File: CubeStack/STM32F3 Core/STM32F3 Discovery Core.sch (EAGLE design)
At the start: 46 parts, among them IC1 FT230XQ, Q1 FC-12M, Q2 MBT3904DW2T1, Q3 MBT3904DW2T1

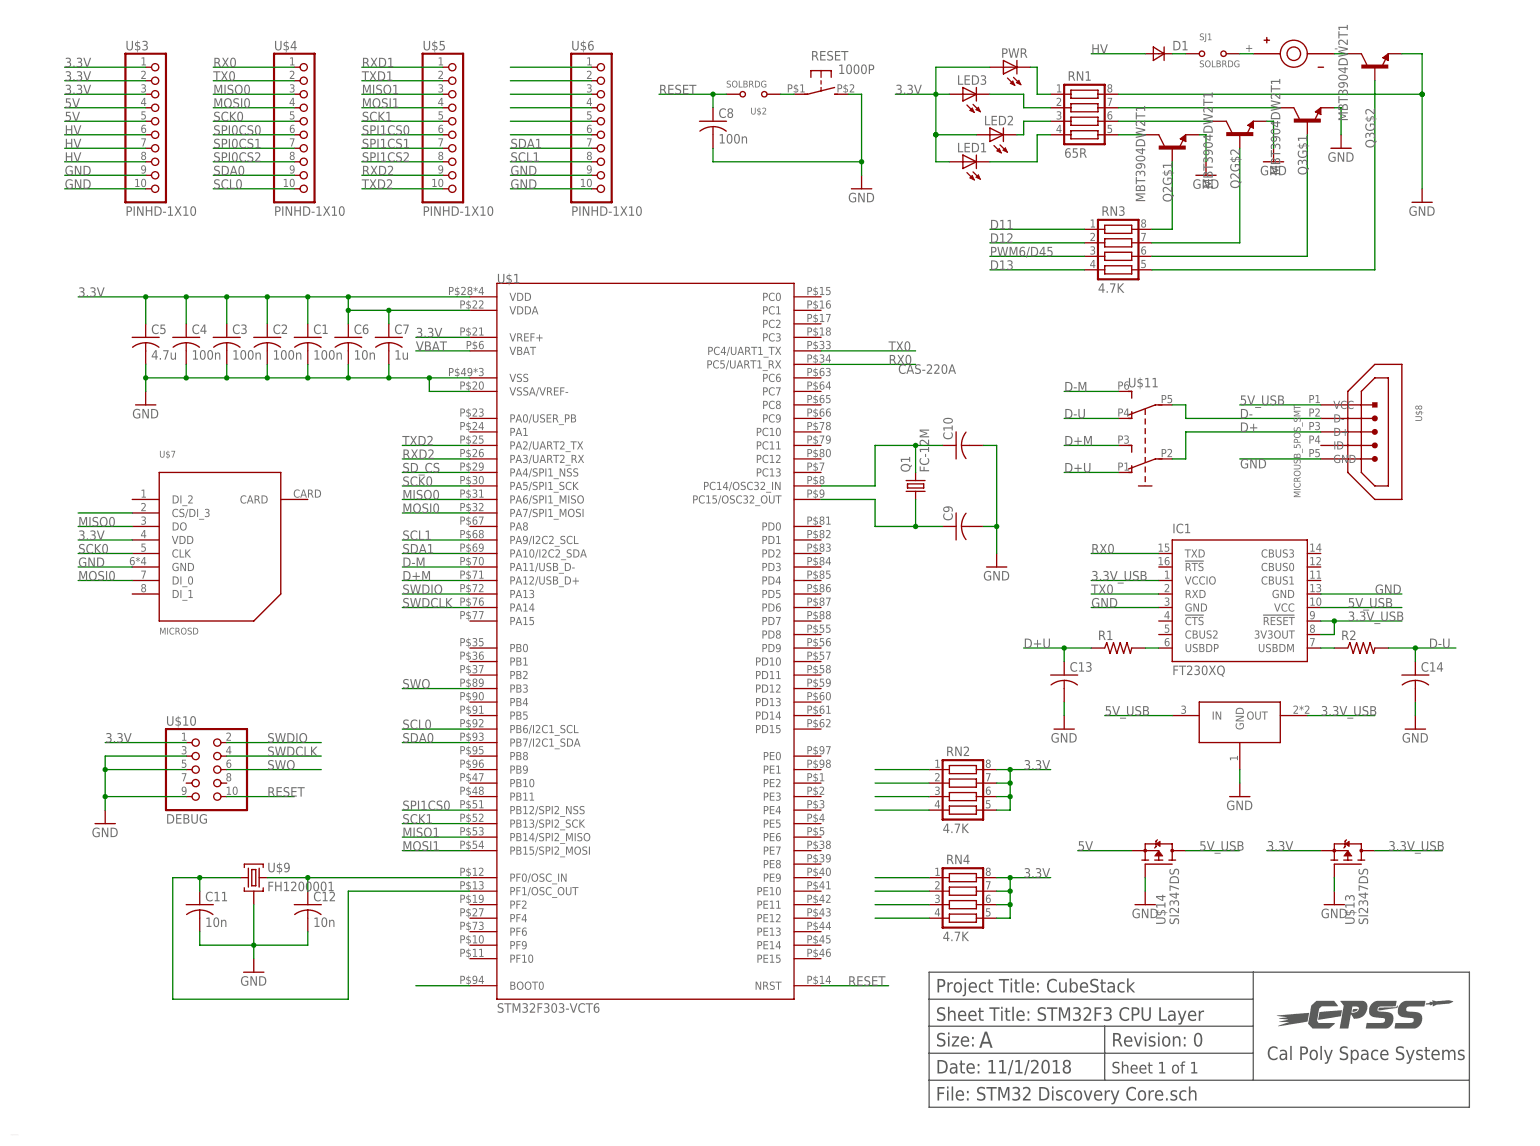
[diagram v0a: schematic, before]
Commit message: Routed PWM, GPIO lines
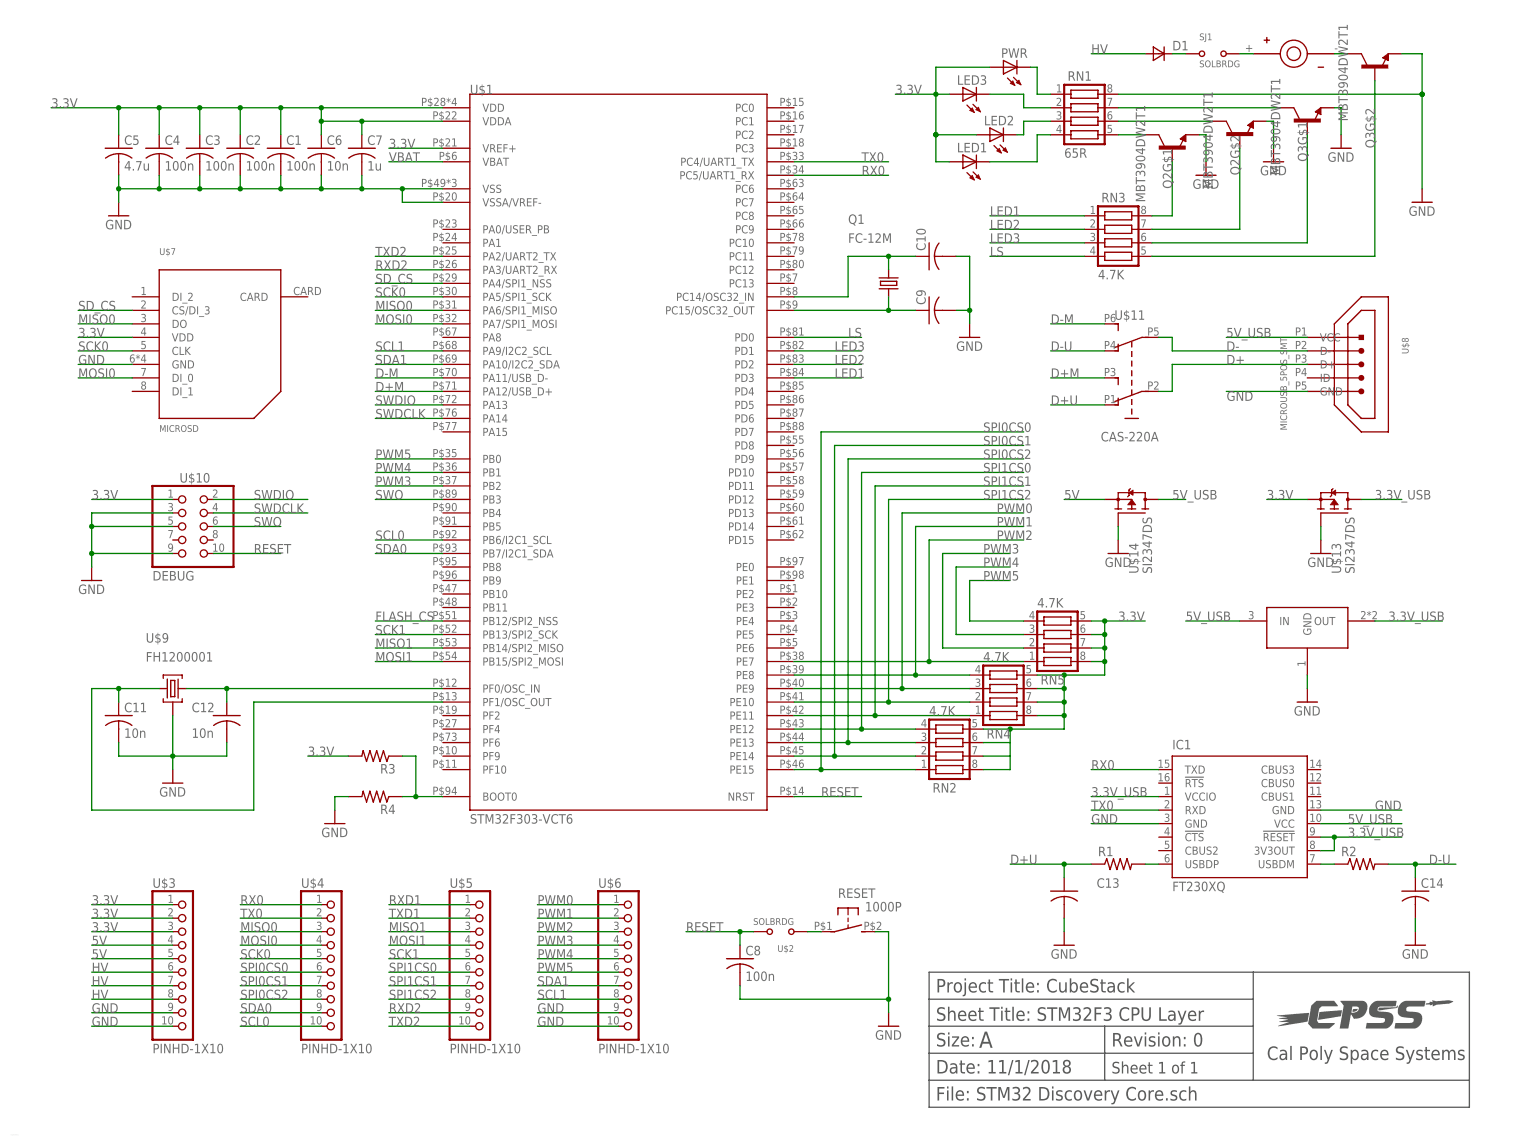
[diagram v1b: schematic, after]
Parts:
- added R3, R4: (no value), resistor:R-US_R0603
- added RN5: 4.7K, resistor-net:CTS742C083
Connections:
- net N$8 renamed L_3_G
- removed net D11: RN3.1
- removed net D12: RN3.2
- removed net D13: RN3.4
- removed net N$12: U$7.CS/DI_3
- removed net N$13: RN2.2
- removed net N$14: RN2.3
- removed net N$15: RN2.4
- removed net N$16: RN4.1
- removed net N$17: RN4.2
- removed net N$18: RN4.3
- removed net N$19: RN4.4
- removed net N$35: U$6.1
- removed net N$36: U$6.2
- removed net N$37: U$6.3
- removed net N$38: U$6.4
- removed net N$39: U$6.5
- removed net N$40: U$6.6
- removed net N$9: RN2.1
- removed net PWM6/D45: RN3.3
- new net FLASH_CS: U$1.PB12/SPI2_NSS
- new net LED1: RN3.1, U$1.PD3
- new net LED2: RN3.2, U$1.PD2
- new net LED3: RN3.3, U$1.PD1
- new net LS: RN3.4, U$1.PD0
- new net N$25: RN2.6
- new net N$26: RN2.7
- new net PWM0: RN4.3, U$1.PE9, U$6.1
- new net PWM1: RN4.4, U$1.PE8, U$6.2
- new net PWM2: RN5.1, U$1.PE7, U$6.3
- new net PWM3: RN5.2, U$1.PB2, U$6.4
- new net PWM4: RN5.3, U$1.PB1, U$6.5
- new net PWM5: RN5.4, U$1.PB0, U$6.6
- net 3.3V: now also R3.2, RN5.5, RN5.6, RN5.7, RN5.8; no longer RN2.6, RN2.7
- net GND: now also R4.2
- net N$20: now also R3.1, R4.1
- net SD_CS: now also U$7.CS/DI_3
- net SPI0CS0: now also RN2.1, U$1.PE15
- net SPI0CS1: now also RN2.2, U$1.PE14
- net SPI0CS2: now also RN2.3, U$1.PE13
- net SPI1CS0: now also RN2.4, U$1.PE12; no longer U$1.PB12/SPI2_NSS
- net SPI1CS1: now also RN4.1, U$1.PE11
- net SPI1CS2: now also RN4.2, U$1.PE10
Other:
- moved on the sheet: C1, C10, C11, C12, C13, C14, C2, C3, C4, C5, C6, C7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

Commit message: Completed STM32 Core to be Reviewed
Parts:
- added C15: (no value), resistor:C-USC0402
- added R5: (no value), resistor:R-US_R0603
- added U1: SST26VF064B, CPSS_IC:SST26VF064B
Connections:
- net RX0 renamed RX1
- net TX0 renamed TX1
- removed net N$25: RN2.6
- removed net N$26: RN2.7
- removed net RXD1: U$5.1
- removed net TXD1: U$5.2
- new net FLASH_HOLD: R5.2, U$1.PB12/SPI2_NSS, U1.HOLD/SIO3
- new net FLASH_WP: U$1.PB10, U1.WP#/SIO2
- new net RXD3: U$1.PD9/UART3_RX, U$5.1
- new net TXD3: U$1.PD8/UART3_TX, U$5.2
- net 3.3V: now also C15.1, R5.1, RN2.6, RN2.7, U1.VDD
- net FLASH_CS: now also U$1.PB11, U1.CE; no longer U$1.PB12/SPI2_NSS
- net GND: now also C15.2, U1.VSS
- net MISO1: now also U1.SO/SIO1
- net MOSI1: now also U1.SI/SIO0
- net SCK1: now also U1.SCK
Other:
- moved on the sheet: C1, C10, C11, C12, C13, C14, C2, C3, C4, C5, C6, C7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

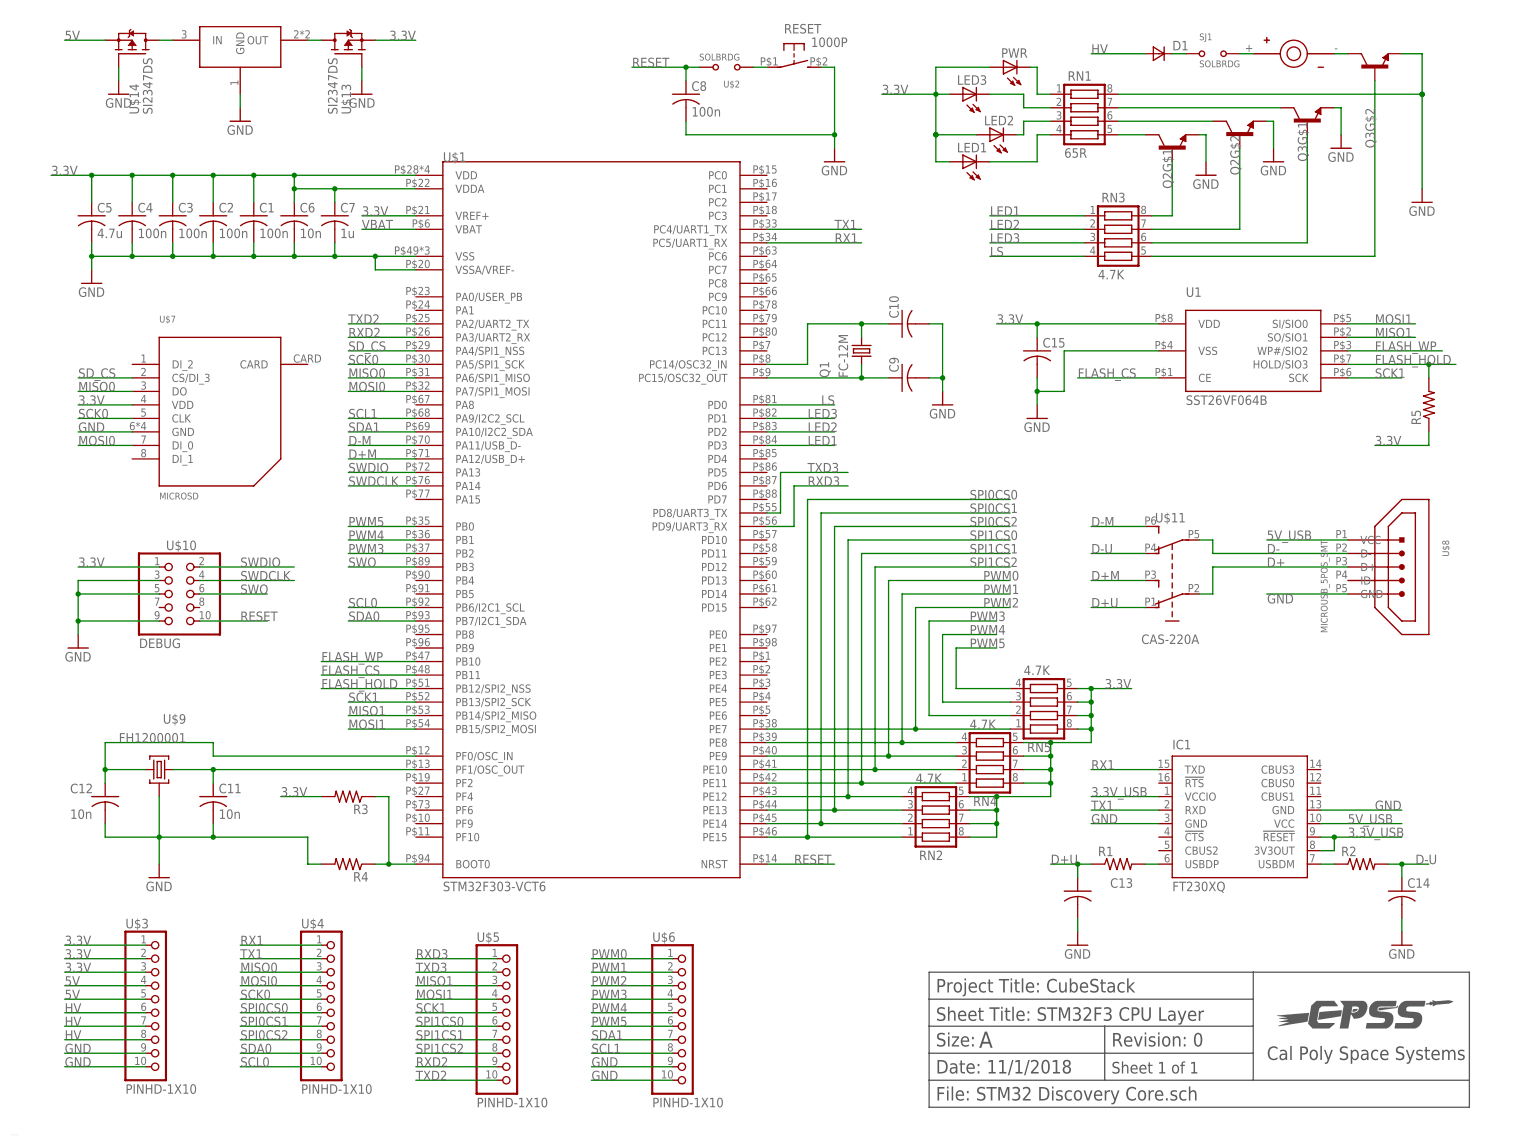
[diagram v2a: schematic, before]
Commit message: Update component names
TODO: Change Resistor/Capacitor names
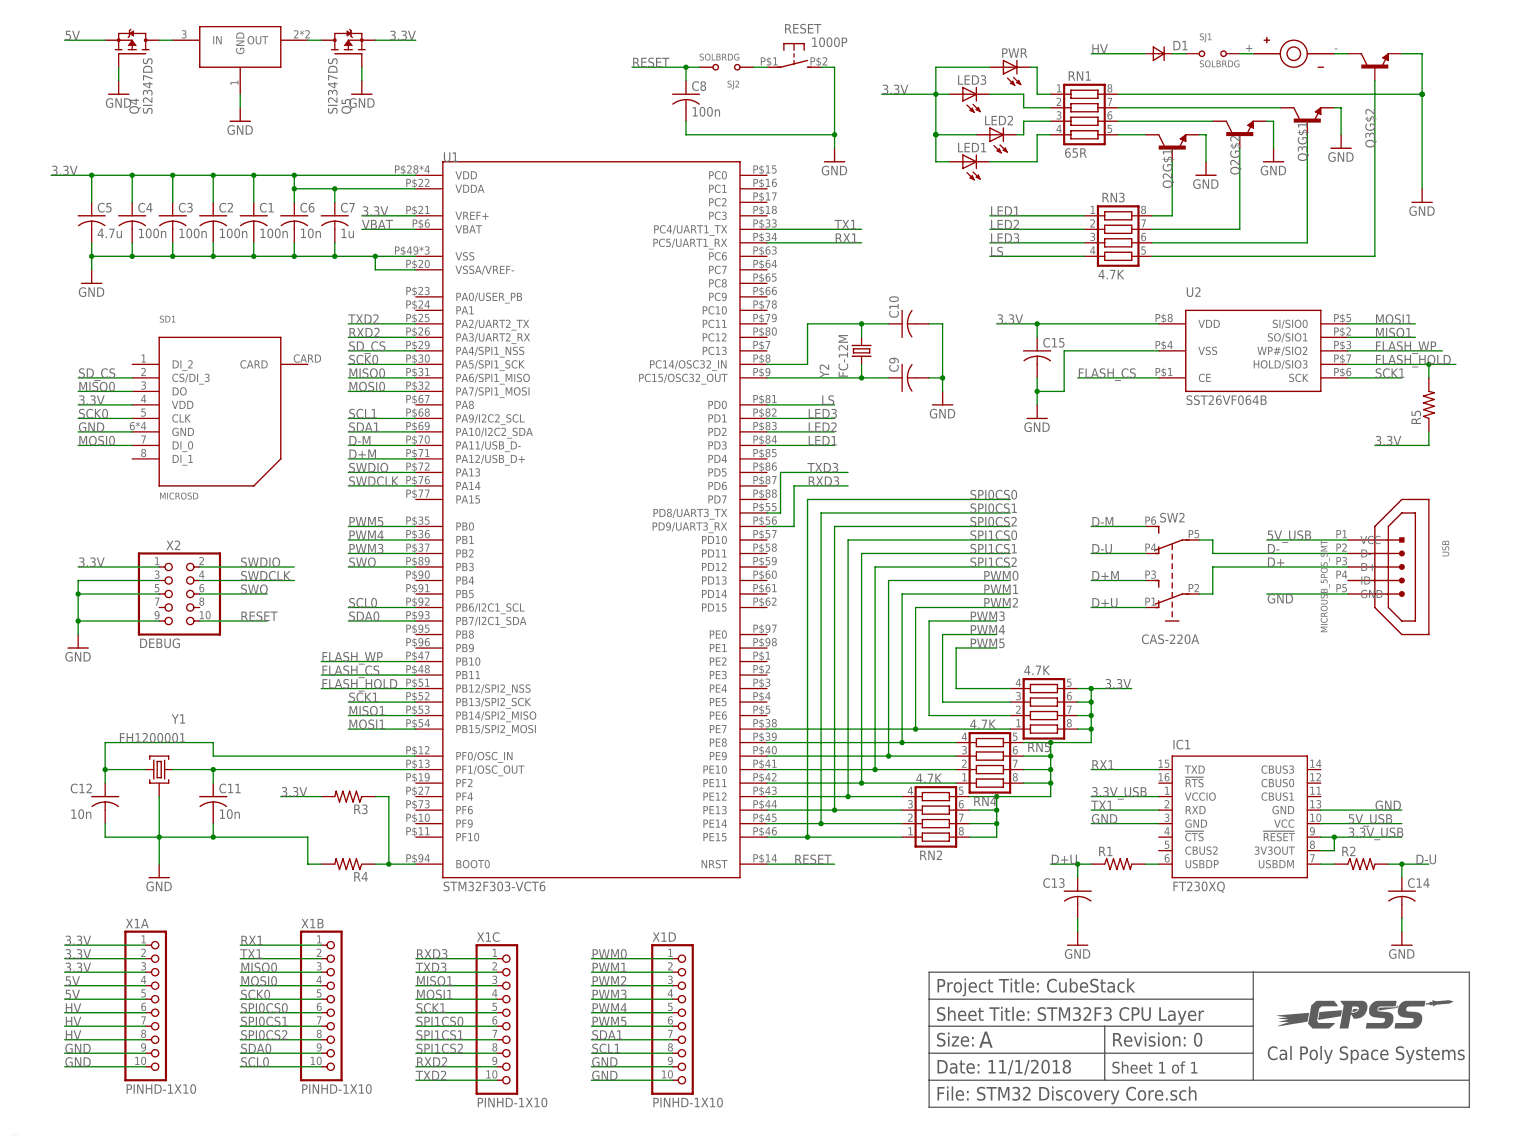
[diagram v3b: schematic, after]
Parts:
- removed U$1: STM32F303-VCT6, CPSS_CPU:STM32F303-VCT6
- added U2: SST26VF064B, CPSS_IC:SST26VF064B
- U1: value SST26VF064B -> STM32F303-VCT6; device CPSS_IC:SST26VF064B -> CPSS_CPU:STM32F303-VCT6
- renumbered Q1 to Y2, U$10 to X2, U$11 to SW2, U$12 to U3, U$13 to Q5, U$14 to Q4, U$2 to SJ2, U$3 to X1A, U$4 to X1B, U$5 to X1C, U$6 to X1D, U$7 to SD1, U$8 to USB, U$9 to Y1
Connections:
- net 3.3V: now also U1.VDDA, U1.VREF+, U2.VDD; no longer U$1.VDD, U$1.VDDA, U$1.VREF+
- net D+M: now also U1.PA12/USB_D+; no longer U$1.PA12/USB_D+
- net D-M: now also U1.PA11/USB_D-; no longer U$1.PA11/USB_D-
- net FLASH_CS: now also U1.PB11, U2.CE; no longer U$1.PB11, U1.CE
- net FLASH_HOLD: now also U1.PB12/SPI2_NSS, U2.HOLD/SIO3; no longer U$1.PB12/SPI2_NSS, U1.HOLD/SIO3
- net FLASH_WP: now also U1.PB10, U2.WP#/SIO2; no longer U$1.PB10, U1.WP#/SIO2
- net GND: now also U1.VSSA/VREF-, U2.VSS; no longer U$1.VSS, U$1.VSSA/VREF-
- net LED1: now also U1.PD3; no longer U$1.PD3
- net LED2: now also U1.PD2; no longer U$1.PD2
- net LED3: now also U1.PD1; no longer U$1.PD1
- net LS: now also U1.PD0; no longer U$1.PD0
- net MISO0: now also U1.PA6/SPI1_MISO; no longer U$1.PA6/SPI1_MISO
- net MISO1: now also U1.PB14/SPI2_MISO, U2.SO/SIO1; no longer U$1.PB14/SPI2_MISO, U1.SO/SIO1
- net MOSI0: now also U1.PA7/SPI1_MOSI; no longer U$1.PA7/SPI1_MOSI
- net MOSI1: now also U1.PB15/SPI2_MOSI, U2.SI/SIO0; no longer U$1.PB15/SPI2_MOSI, U1.SI/SIO0
- net N$2: now also U1.PC14/OSC32_IN; no longer U$1.PC14/OSC32_IN
- net N$20: now also U1.BOOT0; no longer U$1.BOOT0
- net N$4: now also U1.PC15/OSC32_OUT; no longer U$1.PC15/OSC32_OUT
- net N$5: now also U1.PF0/OSC_IN; no longer U$1.PF0/OSC_IN
- net N$6: now also U1.PF1/OSC_OUT; no longer U$1.PF1/OSC_OUT
- net PWM0: now also U1.PE9; no longer U$1.PE9
- net PWM1: now also U1.PE8; no longer U$1.PE8
- net PWM2: now also U1.PE7; no longer U$1.PE7
- net PWM3: now also U1.PB2; no longer U$1.PB2
- net PWM4: now also U1.PB1; no longer U$1.PB1
- net PWM5: now also U1.PB0; no longer U$1.PB0
- net RESET: now also U1.NRST; no longer U$1.NRST
- net RX1: now also U1.PC5/UART1_RX; no longer U$1.PC5/UART1_RX
- net RXD2: now also U1.PA3/UART2_RX; no longer U$1.PA3/UART2_RX
- net RXD3: now also U1.PD9/UART3_RX; no longer U$1.PD9/UART3_RX
- net SCK0: now also U1.PA5/SPI1_SCK; no longer U$1.PA5/SPI1_SCK
- net SCK1: now also U1.PB13/SPI2_SCK, U2.SCK; no longer U$1.PB13/SPI2_SCK, U1.SCK
- net SCL0: now also U1.PB6/I2C1_SCL; no longer U$1.PB6/I2C1_SCL
- net SCL1: now also U1.PA9/I2C2_SCL; no longer U$1.PA9/I2C2_SCL
- net SDA0: now also U1.PB7/I2C1_SDA; no longer U$1.PB7/I2C1_SDA
- net SDA1: now also U1.PA10/I2C2_SDA; no longer U$1.PA10/I2C2_SDA
- net SD_CS: now also U1.PA4/SPI1_NSS; no longer U$1.PA4/SPI1_NSS
- net SPI0CS0: now also U1.PE15; no longer U$1.PE15
- net SPI0CS1: now also U1.PE14; no longer U$1.PE14
- net SPI0CS2: now also U1.PE13; no longer U$1.PE13
- net SPI1CS0: now also U1.PE12; no longer U$1.PE12
- net SPI1CS1: now also U1.PE11; no longer U$1.PE11
- net SPI1CS2: now also U1.PE10; no longer U$1.PE10
- net SWDCLK: now also U1.PA14; no longer U$1.PA14
- net SWDIO: now also U1.PA13; no longer U$1.PA13
- net SWO: now also U1.PB3; no longer U$1.PB3
- net TX1: now also U1.PC4/UART1_TX; no longer U$1.PC4/UART1_TX
- net TXD2: now also U1.PA2/UART2_TX; no longer U$1.PA2/UART2_TX
- net TXD3: now also U1.PD8/UART3_TX; no longer U$1.PD8/UART3_TX
- net VBAT: now also U1.VBAT; no longer U$1.VBAT
